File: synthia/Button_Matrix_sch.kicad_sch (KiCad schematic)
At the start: 84 parts

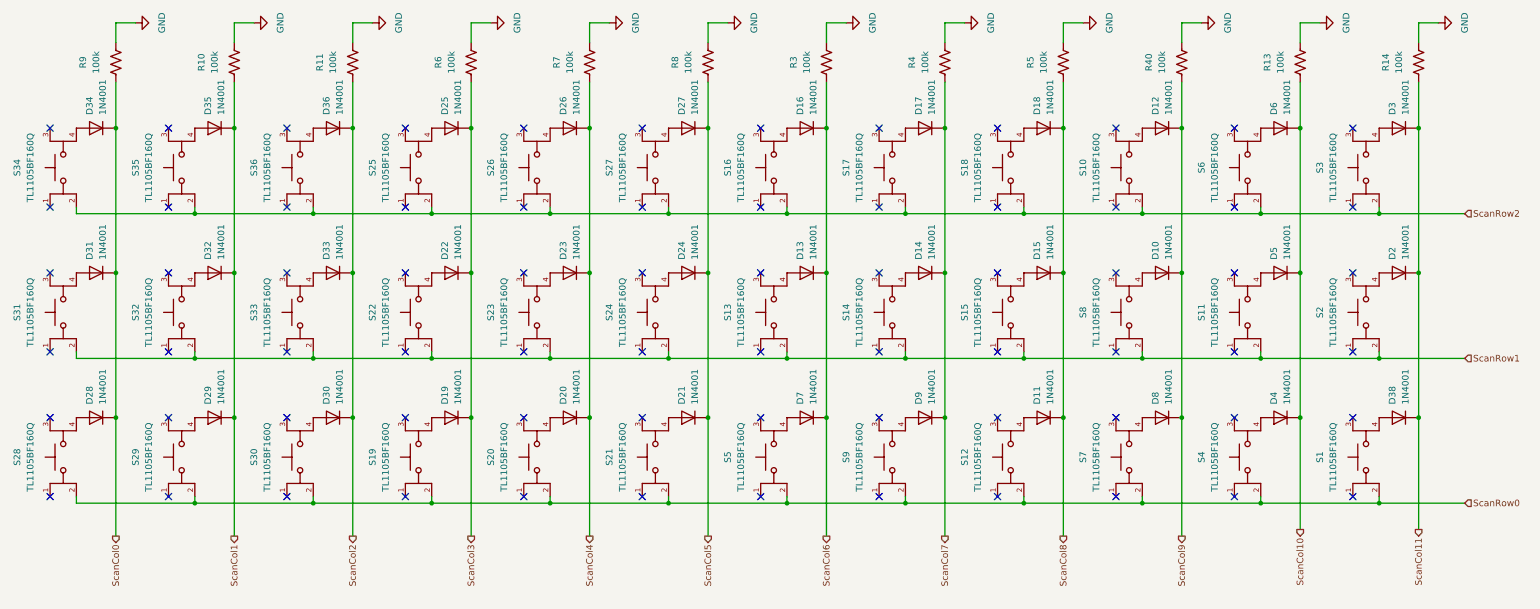
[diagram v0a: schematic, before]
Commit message: Started on the PCB, button matrix is active
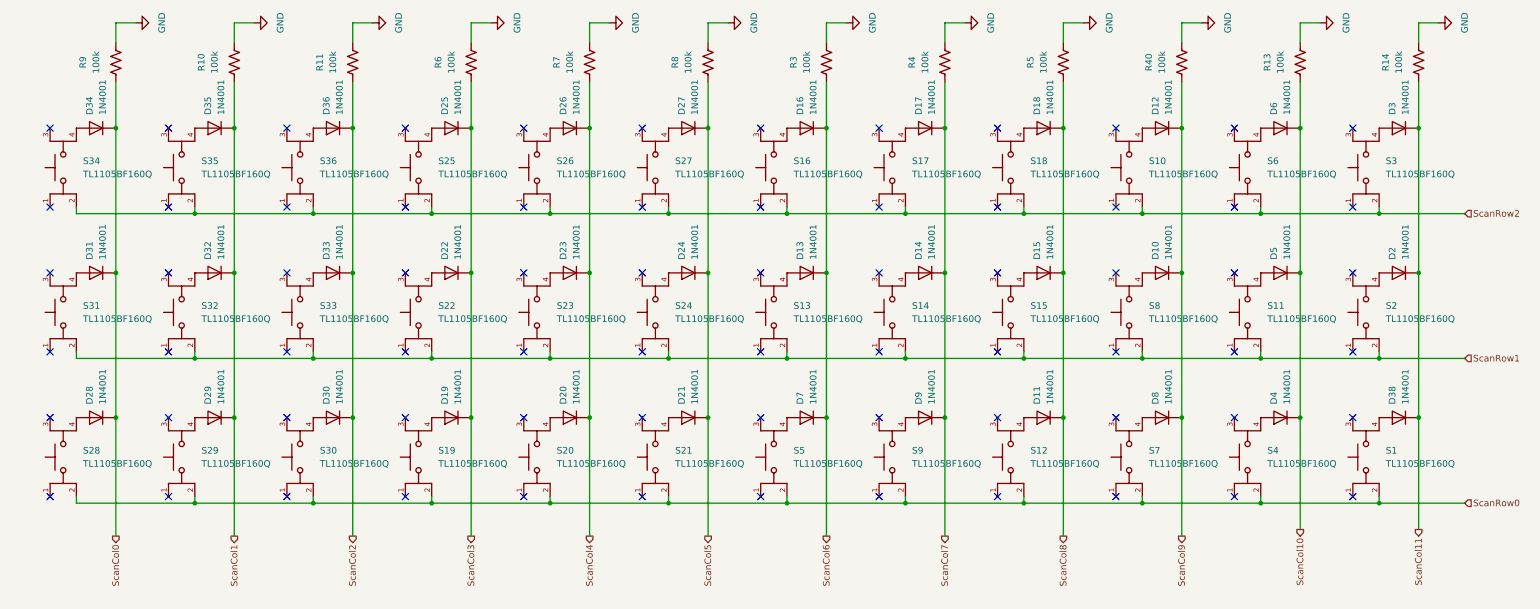
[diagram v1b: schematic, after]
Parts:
- S1, S10, S11, S12, S13, S14, S15, S16, S17, S18, S19, S2, S20, S21, S22, S23, S24, S25, S26, S27, S28, S29, S3, S30, S31, S32, S33, S34, S35, S36, S4, S5, S6, S7, S8, S9: footprint TL1105BF160Q:SW_TL1105BF160Q -> Synthia_footprint_library:SW_TL1105BF160Q; symbol Synthia_Button_Symbol:TL1105BF160Q -> Synthia_Symbol_Library:TL1105BF160Q

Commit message: More updates to the Schematic, ports and solder points added for external components and were wired up
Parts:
- R10, R11, R13, R14, R3, R4, R40, R5, R6, R7, R8, R9: footprint (none) -> Synthia_footprint_library:STA_CF14_STP
